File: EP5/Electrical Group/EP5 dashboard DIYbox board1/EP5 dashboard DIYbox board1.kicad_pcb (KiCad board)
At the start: 4 copper layers, 128.7 x 59.8 mm, 138 parts, among them J1 pedal2-2, J10 Power, J11 pedal1-1, J12 pedal1-2, J2 pedal2-1, J3 MCU, J4 R1, J5 L1, J6 L2, J7 L3, J8 L4, J9 RTD, U1 Seg1, U10 74HC595, U11 74HC595, U12 74HC595, U13 74HC595, U14 74HC595, U15 74HC595, U16 74HC595, U17 74HC595, U18 74HC595, U2 Seg2, U3 Seg3, U4 Seg4, U5 Seg5, U6 Seg6, U7 74HC595, U8 74HC595, U9 74HC595

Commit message: dashboard update left board to latest design
left board is DIYbox board 2
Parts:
- removed R69, R70, R71, R72, R73, R74, R75, R76: 220, Resistor_SMD:R_0603_1608Metric_Pad0.98x0.95mm_HandSolder
- removed the U10 at (163.2, 85.9)
- removed U18: 74HC595, Package_SO:SOIC-16_3.9x9.9mm_P1.27mm
- removed U3: Seg3, Display_7Segment:7SegmentLED_LTS6760_LTS6780
- removed U4: Seg4, Display_7Segment:7SegmentLED_LTS6760_LTS6780
- removed the U9 at (180.1, 85.9)
- added D10: LED, LED_SMD:LED_PLCC_2835, F.Cu at (235.4, 69.1)
- added D11: LED, LED_SMD:LED_PLCC_2835, F.Cu at (239.8, 69.1)
- added D12: LED, LED_SMD:LED_PLCC_2835, F.Cu at (244.1, 69.1)
- added D13: LED, LED_SMD:LED_PLCC_2835, F.Cu at (231.1, 63.6)
- added D14: LED, LED_SMD:LED_PLCC_2835, F.Cu at (235.4, 63.6)
- added D15: LED, LED_SMD:LED_PLCC_2835, F.Cu at (239.8, 63.6)
- added D16: LED, LED_SMD:LED_PLCC_2835, F.Cu at (244.1, 63.6)
- added D9: LED, LED_SMD:LED_PLCC_2835, F.Cu at (231.1, 69.1)
- added U11: 74HC595, Package_SO:SOIC-16_3.9x9.9mm_P1.27mm, B.Cu at (171.6, 83.6)
- added U12: 74HC595, Package_SO:SOIC-16_3.9x9.9mm_P1.27mm, B.Cu at (183.5, 83.6)
- J10, J4, J5, J6, J7, J8: footprint Connector_JST:JST_ZE_SM02B-ZESS-TB_1x02-1MP_P1.50mm_Horizontal -> Connector_JST:JST_XH_S2B-XH-A_1x02_P2.50mm_Horizontal
- J9: footprint Connector_JST:JST_ZE_SM04B-ZESS-TB_1x04-1MP_P1.50mm_Horizontal -> Connector_JST:JST_XH_S4B-XH-A_1x04_P2.50mm_Horizontal
- R33, R34, R35, R36, R37, R38, R39, R40, R41, R42, R43, R44, R45, R46, R47, R48: moved to F.Cu
- U5: value Seg5 -> Seg3
- U6: value Seg6 -> Seg4
- moved R47 120.2 mm to (236.6, 97.8), turned to 0 degrees
- moved R46 117.1 mm to (236.6, 95.3), turned to 0 degrees
- moved R45 116.8 mm to (236.6, 92.8), turned to 0 degrees
- moved D3 113.0 mm to (239.8, 80.2), turned to 90 degrees
- moved R44 112.2 mm to (232.2, 105.3), turned to 0 degrees
- moved R43 109.5 mm to (232.2, 102.8), turned to 0 degrees
- moved R42 108.6 mm to (232.2, 100.3), turned to 0 degrees
- moved R41 108.5 mm to (232.2, 97.8)
- moved D2 106.9 mm to (235.4, 80.2), turned to 90 degrees
- moved R48 105.5 mm to (236.6, 100.3), turned to 0 degrees
- moved D4 104.3 mm to (244.1, 80.2)
- moved D6 101.1 mm to (235.4, 74.7), turned to 90 degrees
- moved D1 100.9 mm to (231.1, 80.2), turned to 90 degrees
- moved R39 94.6 mm to (232.2, 92.8), turned to 0 degrees
- moved D5 94.3 mm to (231.1, 74.7)
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- renumbered U12 to U10, U11 to U9
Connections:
- J3 pad 1: SER -> ButtonR1
- J3 pad 11: ButtonL1 -> OE
- J3 pad 12: ButtonL2 -> GND
- J3 pad 13: ButtonL3 -> SRCLK
- J3 pad 14: ButtonL4 -> GND
- J3 pad 15: ButtonR1 -> SER
- J3 pad 16: ButtonRTD -> GND
- J3 pad 2: GND -> ButtonR2
- J3 pad 3: SRCLK -> ButtonR3
- J3 pad 4: GND -> ButtonR4
- J3 pad 5: SRCLR -> ButtonRTD
- J3 pad 6: GND -> ButtonRTDlight
- J3 pad 9: OE -> SRCLR
- J4 pad 1: ButtonR1 -> ButtonL1
- J5 pad 1: ButtonL1 -> ButtonR1
- J6 pad 1: ButtonL2 -> ButtonR2
- J7 pad 1: ButtonL3 -> ButtonR3
- J8 pad 1: ButtonL4 -> ButtonR4
- R17 pad 2: Net-(U3-B) -> Net-(U5-B)
- R18 pad 2: Net-(U3-A) -> Net-(U5-A)
- R19 pad 2: Net-(U3-C) -> Net-(U5-C)
- R20 pad 2: Net-(U3-D) -> Net-(U5-D)
- R21 pad 2: Net-(U3-E) -> Net-(U5-E)
- R22 pad 2: Net-(U3-F) -> Net-(U5-F)
- R23 pad 2: Net-(U3-G) -> Net-(U5-G)
- R24 pad 2: Net-(U3-DP) -> Net-(U5-DP)
- R25 pad 2: Net-(U4-B) -> Net-(U6-B)
- R26 pad 2: Net-(U4-A) -> Net-(U6-A)
- R27 pad 2: Net-(U4-C) -> Net-(U6-C)
- R28 pad 2: Net-(U4-D) -> Net-(U6-D)
- R29 pad 2: Net-(U4-E) -> Net-(U6-E)
- R30 pad 2: Net-(U4-F) -> Net-(U6-F)
- R31 pad 2: Net-(U4-G) -> Net-(U6-G)
- R32 pad 2: Net-(U4-DP) -> Net-(U6-DP)
- R33 pad 2: Net-(U5-B) -> Net-(D2-A)
- R34 pad 2: Net-(U5-A) -> Net-(D1-A)
- R35 pad 2: Net-(U5-C) -> Net-(D3-A)
- R36 pad 2: Net-(U5-D) -> Net-(D4-A)
- R37 pad 2: Net-(U5-E) -> Net-(D5-A)
- R38 pad 2: Net-(U5-F) -> Net-(D6-A)
- R39 pad 2: Net-(U5-G) -> Net-(D7-A)
- R40 pad 2: Net-(U5-DP) -> Net-(D8-A)
- R41 pad 2: Net-(U6-B) -> Net-(D10-A)
- R42 pad 2: Net-(U6-A) -> Net-(D9-A)
- R43 pad 2: Net-(U6-C) -> Net-(D11-A)
- R44 pad 2: Net-(U6-D) -> Net-(D12-A)
- R45 pad 2: Net-(U6-E) -> Net-(D13-A)
- R46 pad 2: Net-(U6-F) -> Net-(D14-A)
- R47 pad 2: Net-(U6-G) -> Net-(D15-A)
- R48 pad 2: Net-(U6-DP) -> Net-(D16-A)
- U10 pad 1: Net-(U12-QB) -> Net-(U10-QB)
- U10 pad 15: Net-(U12-QA) -> Net-(U10-QA)
- U10 pad 2: Net-(U12-QC) -> Net-(U10-QC)
- U10 pad 3: Net-(U12-QD) -> Net-(U10-QD)
- U10 pad 4: Net-(U12-QE) -> Net-(U10-QE)
- U10 pad 5: Net-(U12-QF) -> Net-(U10-QF)
- U10 pad 6: Net-(U12-QG) -> Net-(U10-QG)
- U10 pad 7: Net-(U12-QH) -> Net-(U10-QH)
- U10 pad 9: Seg6End -> Seg4End
- U13 pad 14: Seg6End -> Seg4End
- U17 pad 9: LEDend5 -> unconnected-(U17-QH'-Pad9)
- U7 pad 14: SER -> Seg6End
- U9 pad 1: Net-(U11-QB) -> Net-(U9-QB)
- U9 pad 14: Seg4End -> Seg2End
- U9 pad 15: Net-(U11-QA) -> Net-(U9-QA)
- U9 pad 2: Net-(U11-QC) -> Net-(U9-QC)
- U9 pad 3: Net-(U11-QD) -> Net-(U9-QD)
- U9 pad 4: Net-(U11-QE) -> Net-(U9-QE)
- U9 pad 5: Net-(U11-QF) -> Net-(U9-QF)
- U9 pad 6: Net-(U11-QG) -> Net-(U9-QG)
- U9 pad 7: Net-(U11-QH) -> Net-(U9-QH)
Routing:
- net OE: track 0.00 -> 202.0 mm
- net RCLK: track 0.00 -> 159.7 mm
- net SRCLK: track 0.00 -> 145.0 mm
- net SRCLR: track 0.00 -> 98.5 mm, vias 0 -> 6
- net Net-(U8-QB): track 51.4 -> 10.0 mm, vias 0 -> 2
- net Net-(U7-QH'): track 46.9 -> 8.39 mm
- net Net-(U12-QH): track 35.5 -> 0.00 mm
- net Net-(U11-QH): track 32.5 -> 0.00 mm
- net Net-(U9-QH): track 28.9 -> 0.00 mm
- net LEDend5: track 27.4 -> 0.00 mm
- net Net-(U12-QC): track 25.2 -> 0.00 mm
- net Net-(U11-QC): track 23.4 -> 0.00 mm
- net Net-(U12-QD): track 22.7 -> 0.00 mm
- net Net-(U11-QD): track 22.3 -> 0.00 mm
- net Net-(U12-QE): track 22.2 -> 0.00 mm
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- added copper zone on B.Cu, net ButtonL1
- removed copper zone on In1.Cu, net +5V
- removed copper zone on B.Cu, net GND
- removed copper zone on In2.Cu, net GND
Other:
- board size 128.7 x 59.8 mm -> 136.1 x 66.7 mm
- copper layers 4 -> 2
- board text removed: "D1"
- board text removed: "D2"

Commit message: 1st dashboard screen board done
and minor pin modification on dashboard left board
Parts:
- added J13: 5V and RTD, Connector_JST:JST_XH_S4B-XH-A_1x04_P2.50mm_Horizontal, B.Cu at (74.3, 85.5)
- J10: value Power -> 12864; footprint Connector_JST:JST_XH_S2B-XH-A_1x02_P2.50mm_Horizontal -> nturt_kicad_lib:12864_1.3_I2C; moved to F.Cu
- J3: footprint Connector_FFC-FPC:TE_1-84952-6_1x16-1MP_P1.0mm_Horizontal -> Connector_JST:JST_XH_S15B-XH-A_1x15_P2.50mm_Horizontal
- R33, R34, R35, R36, R37, R38, R39, R40, R41, R42, R43, R44, R45, R46, R47, R48: moved to B.Cu
- moved D4 137.4 mm to (109.0, 104.9), turned to -90 degrees
- moved D8 137.3 mm to (109.0, 99.1), turned to -90 degrees
- moved D12 137.3 mm to (109.0, 93.2), turned to -90 degrees
- moved D16 137.2 mm to (109.0, 87.4), turned to -90 degrees
- moved D3 117.9 mm to (124.5, 104.9), turned to -90 degrees
- moved D7 117.9 mm to (124.5, 99.1), turned to -90 degrees
- moved D11 117.8 mm to (124.5, 93.2), turned to -90 degrees
- moved D15 117.7 mm to (124.5, 87.4), turned to -90 degrees
- moved J10 100.4 mm to (174.8, 97.0), turned to 0 degrees
- moved D2 98.6 mm to (140.0, 104.9), turned to -90 degrees
- moved D6 98.5 mm to (140.0, 99.1), turned to -90 degrees
- moved D10 98.5 mm to (140.0, 93.2), turned to -90 degrees
- moved D14 98.4 mm to (140.0, 87.4), turned to -90 degrees
- moved D1 79.6 mm to (155.4, 104.9), turned to -90 degrees
- moved D5 79.5 mm to (155.4, 99.1), turned to -90 degrees
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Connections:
- net ButtonR3 renamed ButtonR3_raw
- J3 pad 1: ButtonR1 -> ButtonL1_raw
- J3 pad 10: GND -> OE
- J3 pad 11: OE -> RCLK
- J3 pad 12: GND -> SRCLK
- J3 pad 13: SRCLK -> SRCLR
- J3 pad 14: GND -> SER
- J3 pad 15: SER -> GND
- J3 pad 2: ButtonR2 -> ButtonR4_raw
- J3 pad 4: ButtonR4 -> ButtonR2_raw
- J3 pad 5: ButtonRTD -> ButtonR1_raw
- J3 pad 6: ButtonRTDlight -> GND
- J3 pad 7: RCLK -> SCL
- J3 pad 8: GND -> SDA
- J3 pad 9: SRCLR -> GND
- J4 pad 1: ButtonL1 -> ButtonL1_raw
- J5 pad 1: ButtonR1 -> ButtonR1_raw
- J6 pad 1: ButtonR2 -> ButtonR2_raw
- J8 pad 1: ButtonR4 -> ButtonR4_raw
- J9 pad 3: ButtonRTD -> ButtonRTD_raw
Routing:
- net SRCLR: track 98.5 -> 374.6 mm, vias 6 -> 0
- net OE: track 202.0 -> 392.1 mm
- net SRCLK: track 145.0 -> 313.0 mm
- net RCLK: track 159.7 -> 316.9 mm, vias 0 -> 20
- net SCL: track 0.00 -> 135.4 mm, vias 0 -> 7
- net SDA: track 0.00 -> 129.2 mm, vias 0 -> 7
- net ButtonR4_raw: track 0.00 -> 126.6 mm
- net ButtonR3_raw: track 0.00 -> 114.0 mm
- net ButtonR2_raw: track 0.00 -> 99.3 mm
- net GND: track 0.00 -> 98.8 mm, vias 0 -> 25
- net ButtonR1_raw: track 0.00 -> 81.3 mm
- net Net-(D16-A): track 0.00 -> 73.0 mm, vias 0 -> 1
- net Net-(D4-A): track 0.00 -> 72.3 mm, vias 0 -> 1
- net Net-(D12-A): track 0.00 -> 72.1 mm, vias 0 -> 1
- net Net-(D8-A): track 0.00 -> 72.0 mm, vias 0 -> 1
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- added copper zone on B.Cu, net +5V
- added copper zone on F.Cu, net GND
- removed copper zone on B.Cu, net ButtonL1
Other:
- board size 136.1 x 66.7 mm -> 138.2 x 72.5 mm
- board text removed: "AMS"
- board text removed: "APPS fault"
- board text removed: "ERROR"
- board text removed: "IMD"
- board text removed: "LOW"
- board text removed: "RTD"

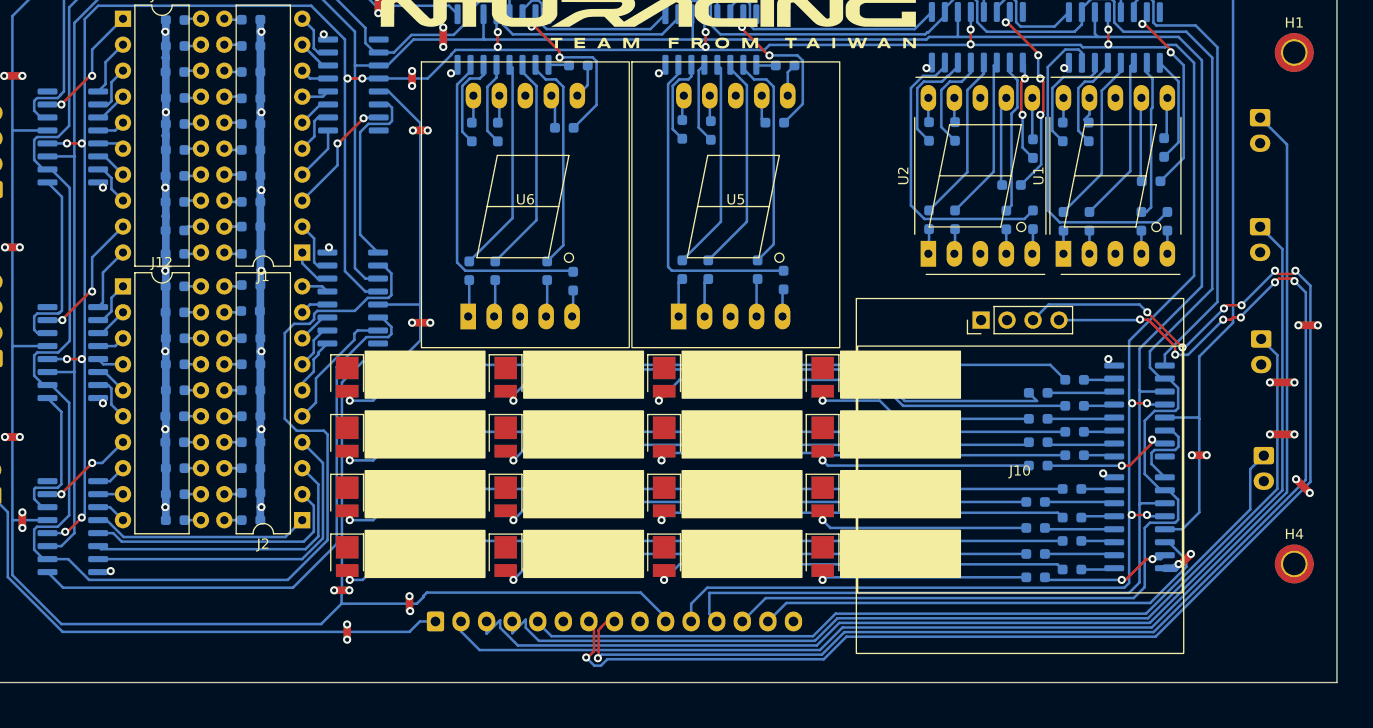
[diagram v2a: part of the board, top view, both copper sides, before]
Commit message: update dashboard boards after Tsou's review
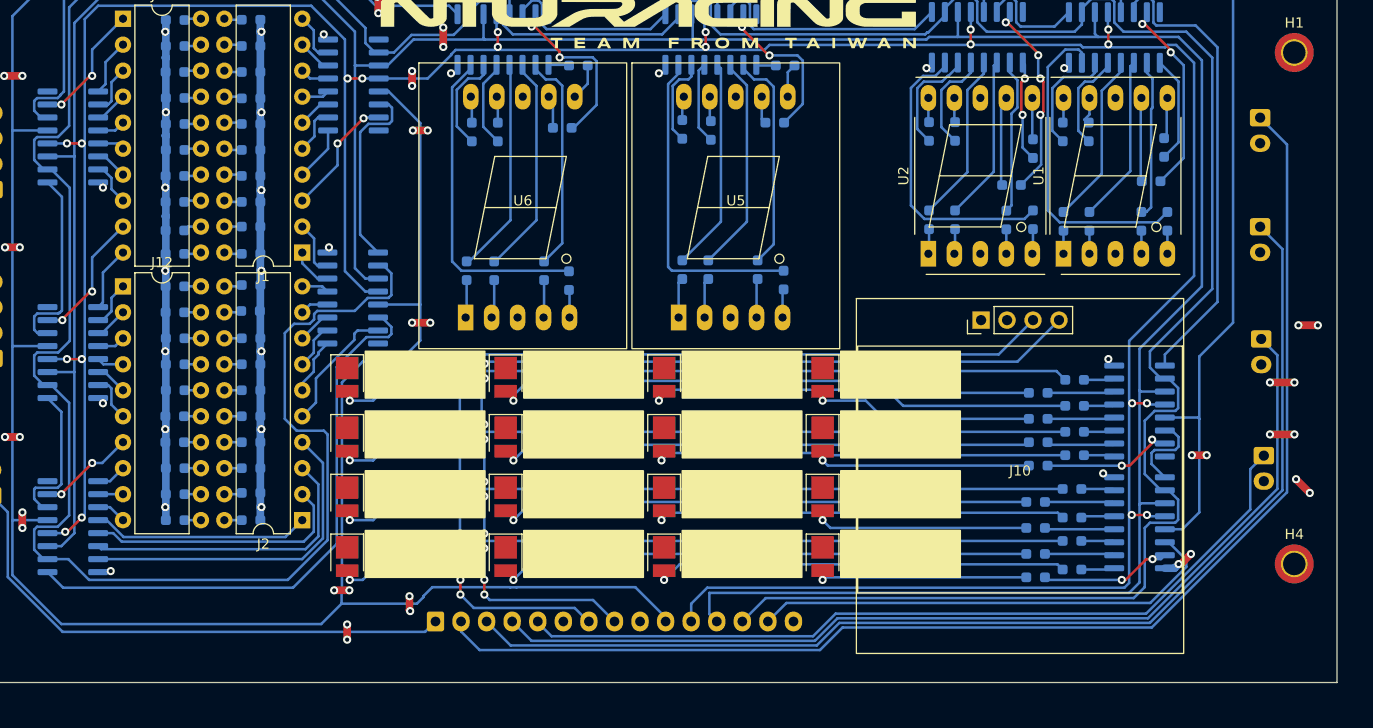
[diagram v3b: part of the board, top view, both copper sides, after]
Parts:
- moved R32 0.41 mm to (130.7, 77.9)
- moved R27 0.30 mm to (128.2, 77.0)
- moved U6 0.27 mm to (126.1, 70.6)
- moved R29 0.25 mm to (120.7, 77.0)
- moved R26 0.20 mm to (130.0, 63.0)
- moved R28 0.10 mm to (123.3, 77.0)
- moved U5 0.10 mm to (147.0, 70.6)
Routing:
- net SCL: track 135.4 -> 94.1 mm, vias 7 -> 10
- net SDA: track 129.2 -> 94.5 mm, vias 7 -> 10
- net Net-(D15-A): track 56.4 -> 53.2 mm
- net ButtonR2_raw: track 99.3 -> 97.1 mm
- net ButtonR3_raw: track 114.0 -> 111.7 mm
- net Net-(D14-A): track 42.7 -> 41.9 mm
- net Net-(U10-QG): track 9.31 -> 9.84 mm

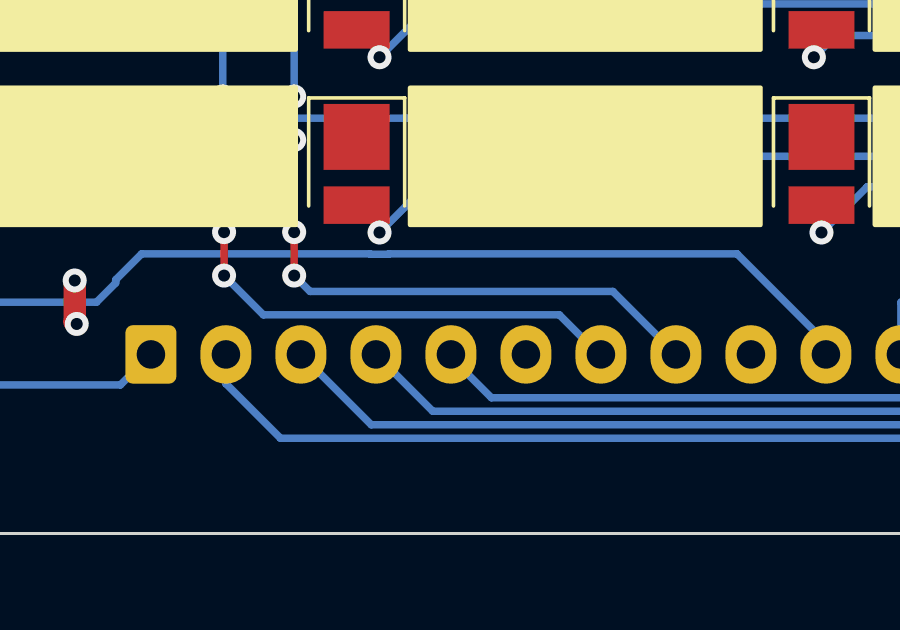
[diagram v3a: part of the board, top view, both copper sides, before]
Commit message: update all boards after Tsou's second review
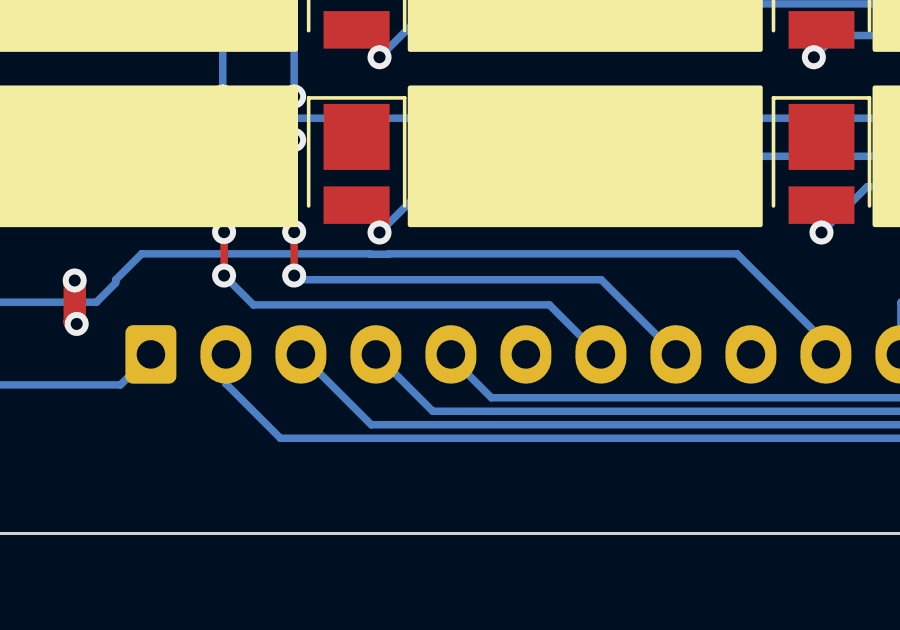
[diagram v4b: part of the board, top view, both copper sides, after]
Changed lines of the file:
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@@
     (comment 1 "郭哲明")
     (comment 2 "electrical group")
+    (comment 3 "1.6T/1oz/綠色防焊/白色文字/無鉛噴錫/各5pcs")
   )
   (layers
@@
   (segment (start 119.9896 91.8028) (end 119.9896 91.9855) (width 0.25) (layer "B.Cu") (net 201))
   (segment (start 119.9968 99.0297) (end 119.9896 99.0225) (width 0.25) (layer "B.Cu") (net 201))
-  (segment (start 121.3479 109.9312) (end 131.2164 109.9312) (width 0.25) (layer "B.Cu") (net 201))
-  (segment (start 120.0404 108.6237) (end 121.3479 109.9312) (width 0.25) (layer "B.Cu") (net 201))
   (segment (start 119.9824 91.7956) (end 119.9896 91.8028) (width 0.25) (layer "B.Cu") (net 201))
   (segment (start 119.9968 102.6535) (end 119.9968 99.0297) (width 0.25) (layer "B.Cu") (net 201))
   (segment (start 119.9896 93.4345) (end 119.9896 97.5735) (width 0.25) (layer "B.Cu") (net 201))
-  (segment (start 132.5372 111.252) (end 132.602 111.252) (width 0.25) (layer "B.Cu") (net 201))
   (segment (start 120.0404 107.1747) (end 119.9968 107.1311) (width 0.25) (layer "B.Cu") (net 201))
+  (segment (start 120.0404 108.6237) (end 121.0177 109.601) (width 0.25) (layer "B.Cu") (net 201))
   (segment (start 119.9896 87.4909) (end 119.9824 87.4981) (width 0.25) (layer "B.Cu") (net 201))
   (segment (start 119.9824 87.4981) (end 119.9824 91.7956) (width 0.25) (layer "B.Cu") (net 201))
+  (segment (start 121.0177 109.601) (end 130.8862 109.601) (width 0.25) (layer "B.Cu") (net 201))
+  (segment (start 132.5372 111.252) (end 132.602 111.252) (width 0.25) (layer "B.Cu") (net 201))
+  (segment (start 130.8862 109.601) (end 132.5372 111.252) (width 0.25) (layer "B.Cu") (net 201))
   (segment (start 120.8907 85.1408) (end 172.6692 85.1408) (width 0.25) (layer "B.Cu") (net 201))
   (segment (start 119.9968 107.1311) (end 119.9968 104.1025) (width 0.25) (layer "B.Cu") (net 201))
-  (segment (start 131.2164 109.9312) (end 132.5372 111.252) (width 0.25) (layer "B.Cu") (net 201))
   (segment (start 119.9896 86.0419) (end 120.8907 85.1408) (width 0.25) (layer "B.Cu") (net 201))
   (segment (start 122.3772 107.1747) (end 122.3772 108.6237) (width 0.25) (layer "F.Cu") (net 202))
@@
   (via (at 122.3772 91.9855) (size 0.8) (drill 0.4) (layers "F.Cu" "B.Cu") (net 202))
   (segment (start 122.428 87.4909) (end 122.116 87.8029) (width 0.25) (layer "B.Cu") (net 202))
+  (segment (start 122.3772 108.6237) (end 122.5163 108.7628) (width 0.25) (layer "B.Cu") (net 202))
+  (segment (start 122.5163 108.7628) (end 132.6128 108.7628) (width 0.25) (layer "B.Cu") (net 202))
   (segment (start 178.562 81.788) (end 174.498 85.852) (width 0.25) (layer "B.Cu") (net 202))
   (segment (start 122.682 85.852) (end 122.4921 86.0419) (width 0.25) (layer "B.Cu") (net 202))
+  (segment (start 132.6128 108.7628) (end 135.102 111.252) (width 0.25) (layer "B.Cu") (net 202))
   (segment (start 174.498 85.852) (end 122.682 85.852) (width 0.25) (layer "B.Cu") (net 202))
-  (segment (start 133.0025 109.1525) (end 135.102 111.252) (width 0.25) (layer "B.Cu") (net 202))
-  (segment (start 122.906 109.1525) (end 133.0025 109.1525) (width 0.25) (layer "B.Cu") (net 202))
   (segment (start 122.3772 104.1025) (end 122.3772 107.1747) (width 0.25) (layer "B.Cu") (net 202))
   (segment (start 122.116 91.7243) (end 122.3772 91.9855) (width 0.25) (layer "B.Cu") (net 202))
@@
   (segment (start 122.4921 86.0419) (end 122.428 86.0419) (width 0.25) (layer "B.Cu") (net 202))
   (segment (start 122.3772 99.0225) (end 122.3772 102.6535) (width 0.25) (layer "B.Cu") (net 202))
-  (segment (start 122.3772 108.6237) (end 122.906 109.1525) (width 0.25) (layer "B.Cu") (net 202))
   (segment (start 73.016 79.238) (end 73.016 65.328) (width 0.25) (layer "B.Cu") (net 203))
   (segment (start 73.016 65.328) (end 74.316 64.028) (width 0.25) (layer "B.Cu") (net 203))
